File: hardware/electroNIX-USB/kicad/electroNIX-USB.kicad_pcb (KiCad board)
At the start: 2 copper layers, 102 x 66 mm, 127 parts, among them J1 USB-C (USB 2.0), Q1 MMBT3904, Q10 MMBTA42, Q11 MMBTA92, Q12 MMBTA42, Q13 MMBTA42, Q14 MMBTA42, Q15 MMBTA42, Q16 MMBTA42, Q17 MMBTA42, Q18 MMBTA42, Q19 MMBTA42, Q2 MMBT3904, Q20 MMBTA42, Q21 MMBTA42, Q22 MMBTA42, Q23 MMBTA42, Q3 IRLR3110ZPBF, Q4 MMBTA42, Q5 MMBTA92, Q6 MMBTA42, Q7 MMBTA92, Q8 MMBTA42, Q9 MMBTA92, U1 USBLC6-2SC6, U2 AMS1117-3.3, U3 CH340C, U4 ESP32-WROOM-32E-N4

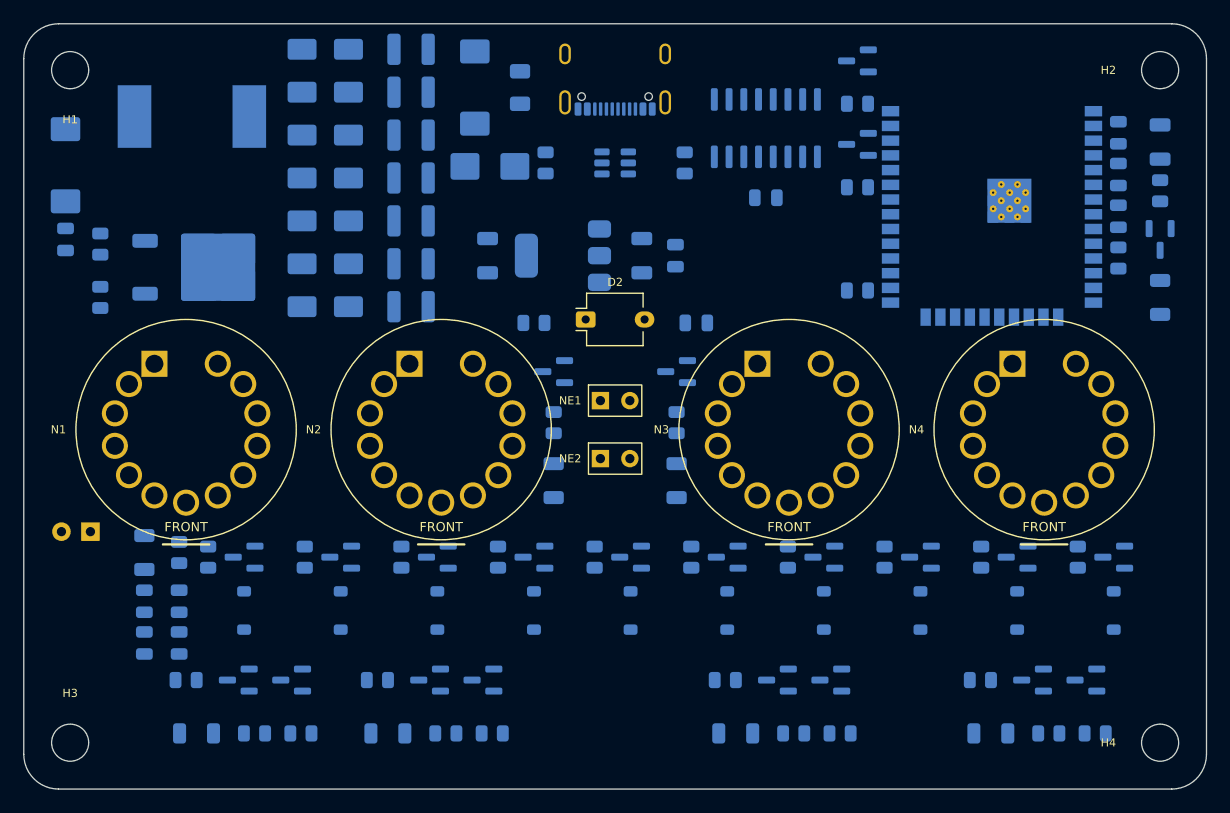
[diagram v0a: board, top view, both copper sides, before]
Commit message: electroNIX-USB: clash-free silkscreen, DRC clean-up
- References at 0.8 mm, auto-placed clear of other references, part
  silkscreen, pads and the board edge (inside the part between pads as a
  last resort)
- ESP32: replace the stock 48 mm keep-out zone/courtyard with a body
  courtyard + antenna rule area; module 0.3 mm inside the edge; min drill
  0.2 mm for its exposed-pad vias
- Tube footprints: round pad 1 (the square pad crowded pad 2) with a
  silk pin-1 dot
- KBIAS columns spaced out slightly

DRC on both placed boards: only the stock USB-C footprint's peg-to-pad
clearance remains (plus the expected unrouted nets).

Co-Authored-By: Claude Opus 5.5 <noreply@anthropic.com>
Claude-Session: https://claude.ai/code/session_01AFMfevKEKDGbci8uJGhf4W
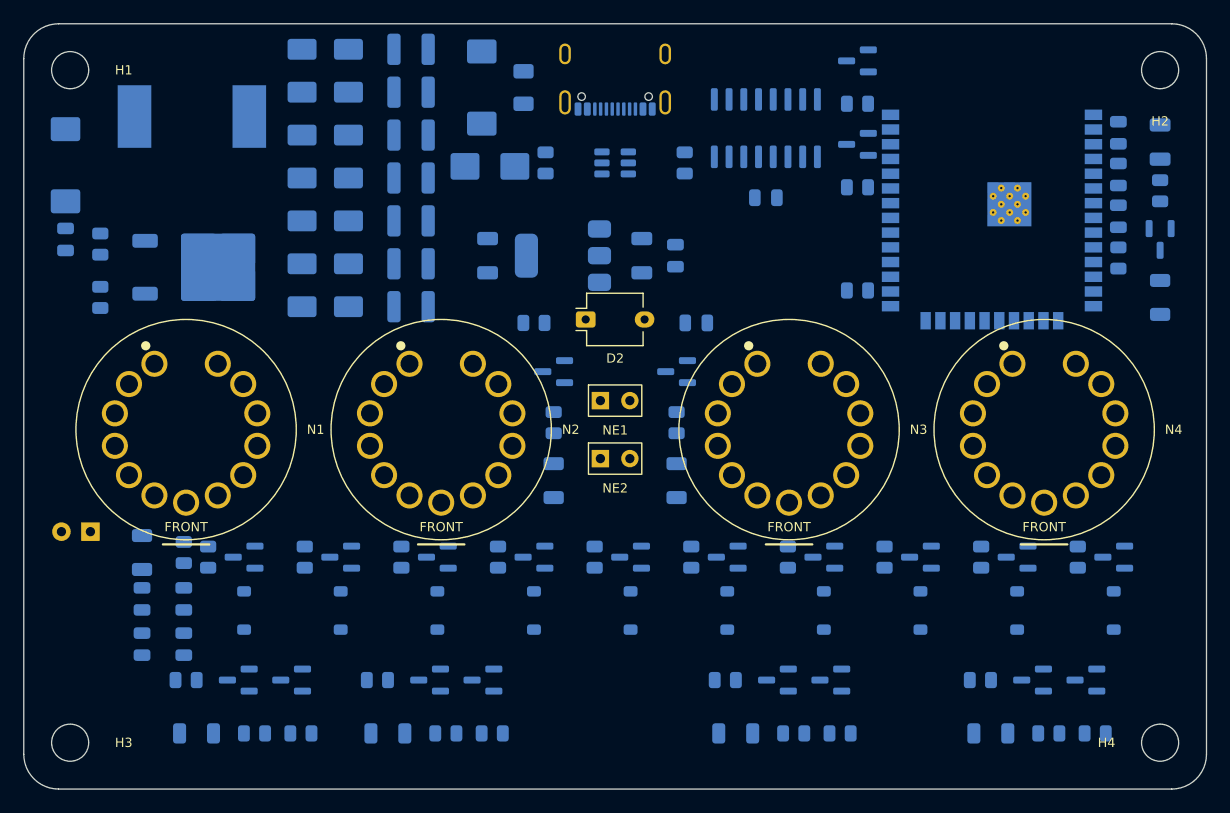
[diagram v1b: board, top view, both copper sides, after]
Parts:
- moved C1 0.60 mm to (139.5, 105.5)
- moved C22 0.45 mm to (113.8, 149.6)
- moved C24 0.41 mm to (113.8, 153.5)
- moved R43 0.40 mm to (113.8, 145.6)
- moved U4 0.31 mm to (183.5, 116.1)
- moved F1 0.30 mm to (143.1, 105.5)
- moved C21 0.28 mm to (110.2, 149.6)
- moved C23 0.22 mm to (110.2, 153.5)
- moved R42 0.20 mm to (110.2, 145.6)

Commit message: electroNIX-USB: keep every reference beside or inside its own part
Label placement now only accepts spots within ~1 mm of the part and
closer to it than to any other part; otherwise the reference goes inside
the footprint between the pads. Hard cases are retried first. The KBIAS
network moved under the colon, and the auto-reset strip was spaced out
so every label fits at 0.8 mm. DRC: only the stock USB-C footprint item.

Co-Authored-By: Claude Opus 5.5 <noreply@anthropic.com>
Claude-Session: https://claude.ai/code/session_01AFMfevKEKDGbci8uJGhf4W
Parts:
- moved C23 43.1 mm to (152.6, 161.0)
- moved C24 42.7 mm to (155.8, 161.0)
- moved R43 41.7 mm to (154.0, 156.6), turned to 180 degrees
- moved R42 39.4 mm to (148.0, 156.6), turned to 180 degrees
- moved C21 37.8 mm to (146.2, 161.0)
- moved C22 37.4 mm to (149.4, 161.0)
- moved D11 2.50 mm to (116.5, 150.6)
- moved Q12 2.50 mm to (116.5, 146.0)
- moved R28 2.50 mm to (113.4, 146.0)
- moved R29 2.22 mm to (122.0, 146.0)
- moved D12 2.22 mm to (125.1, 150.6)
- moved Q13 2.22 mm to (125.1, 146.0)
- moved D13 1.94 mm to (133.7, 150.6)
- moved Q14 1.94 mm to (133.7, 146.0)
- moved R30 1.94 mm to (130.6, 146.0)
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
